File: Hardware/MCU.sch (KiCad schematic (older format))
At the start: 11 parts, among them J1 HDR, SW1 SW_Push, SW2 SW_Push, U5 ESP32-WROOM-32D

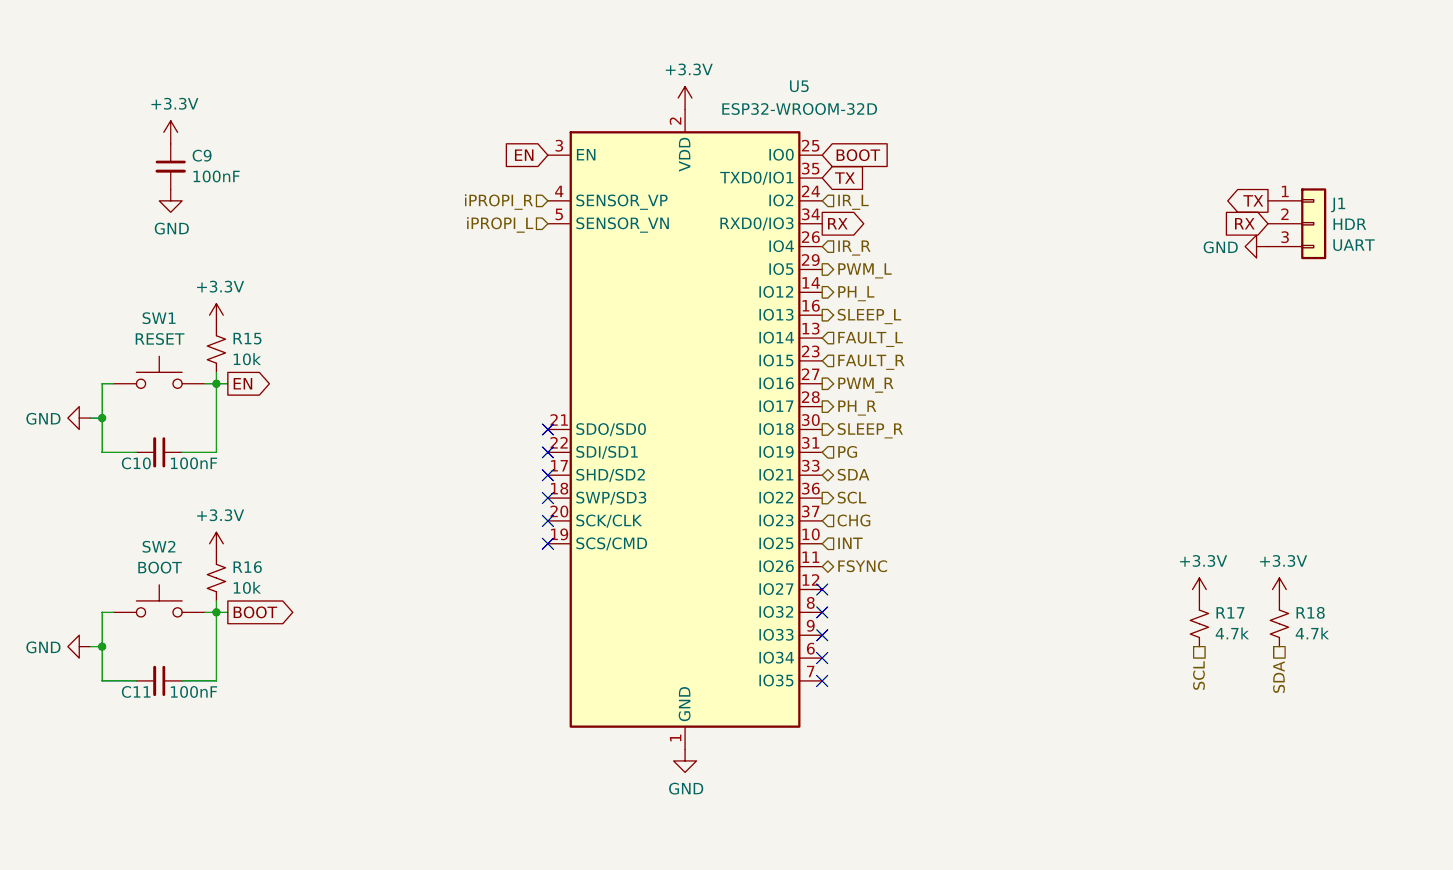
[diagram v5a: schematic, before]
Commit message: Schematic updated, USB comms circuit added
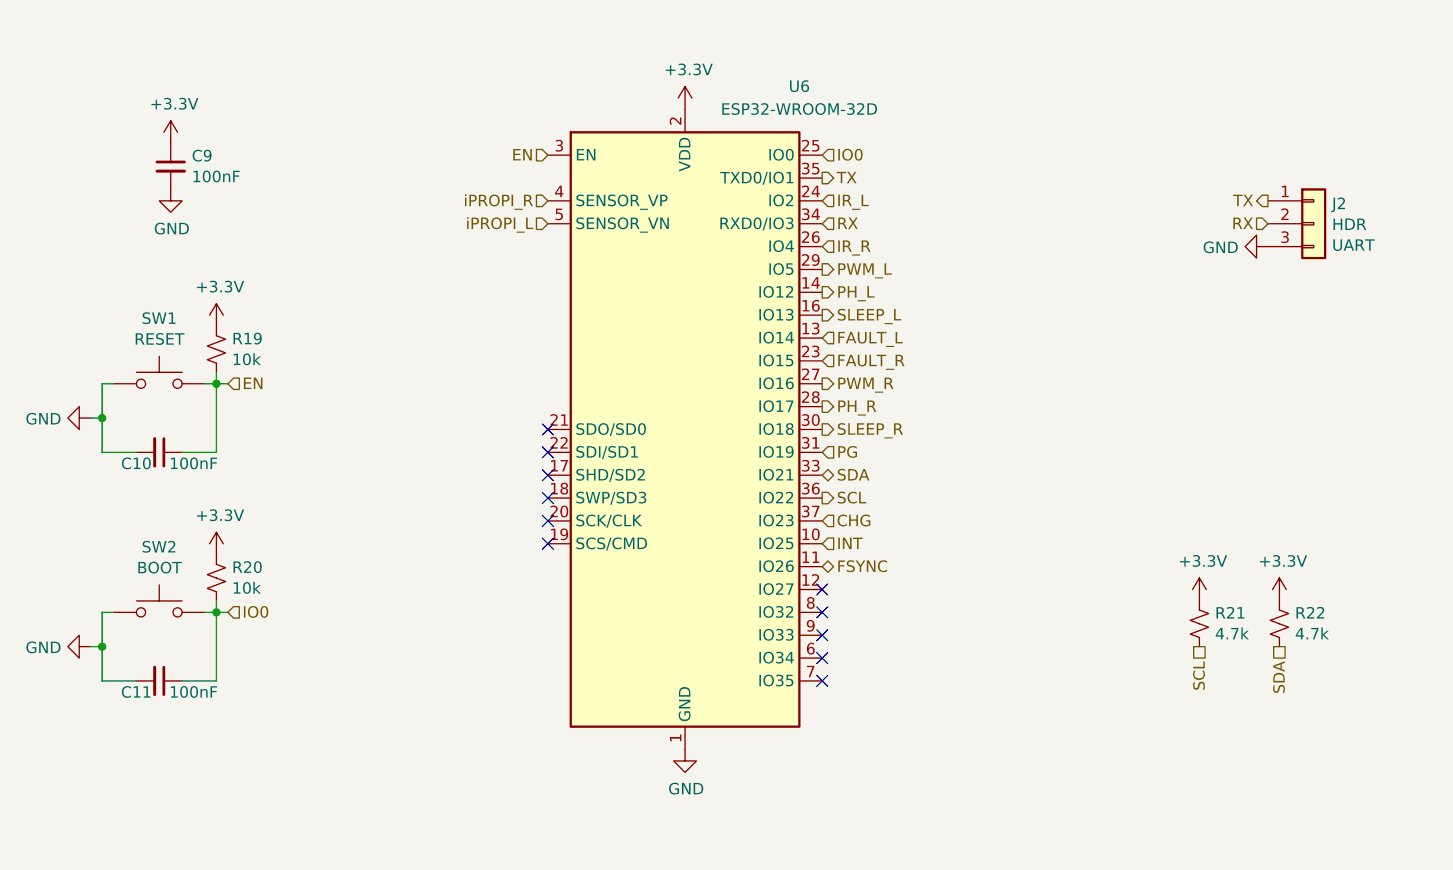
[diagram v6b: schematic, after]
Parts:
- J2: renamed from J1; footprint (none) -> Connector_PinSocket_2.54mm:PinSocket_1x03_P2.54mm_Vertical
- R21: renamed from R17; footprint Resistor_SMD:R_0603_1608Metric -> Resistor_SMD:R_0805_2012Metric
- R22: renamed from R18; footprint Resistor_SMD:R_0603_1608Metric -> Resistor_SMD:R_0805_2012Metric
- renumbered R15 to R19, R16 to R20, U5 to U6
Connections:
- net BOOT renamed IO0
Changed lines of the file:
@@
 $Descr A4 11693 8268
 encoding utf-8
-Sheet 6 9
+Sheet 6 11
 Title ""
 Date ""
@@
 AR Path="/5EA2026E/5FF09BD0" Ref="#PWR?"  Part="1"
 AR Path="/5FF09BD0" Ref="#PWR?"  Part="1"
-AR Path="/5FEFFC20/5FF09BD0" Ref="#PWR035"  Part="1"
-F 0 "#PWR035" H 3750 2400 50  0001 C CNN
+AR Path="/5FEFFC20/5FF09BD0" Ref="#PWR039"  Part="1"
+F 0 "#PWR039" H 3750 2400 50  0001 C CNN
 F 1 "+3.3V" H 3765 2723 50  0000 C CNN
 F 2 "" H 3750 2550 50  0001 C CNN
@@
 	1    0    0    -1
 $EndComp
-Text GLabel 4000 3600 2    50   Output ~ 0
-EN
 $Comp
 L Device:C_Small C?
@@
 Wire Wire Line
 	3450 4600 3500 4600
-Text GLabel 4000 4600 2    50   Output ~ 0
-BOOT
 NoConn ~ 5400 3800
 NoConn ~ 5400 3900
@@
 NoConn ~ 5400 4200
 NoConn ~ 5400 4300
-Text GLabel 5400 2600 0    50   Input ~ 0
-EN
-Text GLabel 6600 2600 2    50   Input ~ 0
-BOOT
-$Comp
-L power:GND #PWR044
+$Comp
+L power:GND #PWR048
 U 1 1 5FF09BF4
 P 6000 5200
-F 0 "#PWR044" H 6000 4950 50  0001 C CNN
+F 0 "#PWR048" H 6000 4950 50  0001 C CNN
 F 1 "GND" H 6005 5027 50  0000 C CNN
 F 2 "" H 6000 5200 50  0001 C CNN
@@
 AR Path="/5EA2026E/5FF09C08" Ref="#PWR?"  Part="1"
 AR Path="/5FF09C08" Ref="#PWR?"  Part="1"
-AR Path="/5FEFFC20/5FF09C08" Ref="#PWR036"  Part="1"
-F 0 "#PWR036" H 3750 2500 50  0001 C CNN
+AR Path="/5FEFFC20/5FF09C08" Ref="#PWR040"  Part="1"
+F 0 "#PWR040" H 3750 2500 50  0001 C CNN
 F 1 "GND" H 3755 2577 50  0000 C CNN
 F 2 "" H 3750 2750 50  0001 C CNN
@@
 AR Path="/5EA2026E/5FF09C14" Ref="#PWR?"  Part="1"
 AR Path="/5FF09C14" Ref="#PWR?"  Part="1"
-AR Path="/5FEFFC20/5FF09C14" Ref="#PWR038"  Part="1"
-F 0 "#PWR038" H 3950 3200 50  0001 C CNN
+AR Path="/5FEFFC20/5FF09C14" Ref="#PWR042"  Part="1"
+F 0 "#PWR042" H 3950 3200 50  0001 C CNN
 F 1 "+3.3V" H 3965 3523 50  0000 C CNN
 F 2 "" H 3950 3350 50  0001 C CNN
@@
 AR Path="/5EA2026E/5FF09C1A" Ref="R?"  Part="1"
 AR Path="/5FF09C1A" Ref="R?"  Part="1"
-AR Path="/5FEFFC20/5FF09C1A" Ref="R15"  Part="1"
-F 0 "R15" H 4018 3496 50  0000 L CNN
+AR Path="/5FEFFC20/5FF09C1A" Ref="R19"  Part="1"
+F 0 "R19" H 4018 3496 50  0000 L CNN
 F 1 "10k" H 4018 3405 50  0000 L CNN
 F 2 "Resistor_SMD:R_0805_2012Metric" H 3950 3450 50  0001 C CNN
@@
 	3950 3550 3950 3600
 $Comp
-L power:GND #PWR039
+L power:GND #PWR043
 U 1 1 5FF09C21
 P 3400 3750
-F 0 "#PWR039" H 3400 3500 50  0001 C CNN
+F 0 "#PWR043" H 3400 3500 50  0001 C CNN
 F 1 "GND" V 3405 3622 50  0000 R CNN
 F 2 "" H 3400 3750 50  0001 C CNN
@@
 	3450 3750 3450 3600
 $Comp
-L power:GND #PWR043
+L power:GND #PWR047
 U 1 1 5FF09C2A
 P 3400 4750
-F 0 "#PWR043" H 3400 4500 50  0001 C CNN
+F 0 "#PWR047" H 3400 4500 50  0001 C CNN
 F 1 "GND" V 3405 4622 50  0000 R CNN
 F 2 "" H 3400 4750 50  0001 C CNN
@@
 	3450 4750 3450 4600
 $Comp
-L power:+3.3V #PWR034
+L power:+3.3V #PWR038
 U 1 1 5FF09C33
 P 6000 2400
-F 0 "#PWR034" H 6000 2250 50  0001 C CNN
+F 0 "#PWR038" H 6000 2250 50  0001 C CNN
 F 1 "+3.3V" H 6015 2573 50  0000 C CNN
 F 2 "" H 6000 2400 50  0001 C CNN
@@
 $EndComp
 $Comp
-L Device:R_Small_US R18
+L Device:R_Small_US R22
 U 1 1 5FF09C39
 P 8600 4650
-F 0 "R18" H 8668 4696 50  0000 L CNN
+F 0 "R22" H 8668 4696 50  0000 L CNN
 F 1 "4.7k" H 8668 4605 50  0000 L CNN
-F 2 "Resistor_SMD:R_0603_1608Metric" H 8600 4650 50  0001 C CNN
+F 2 "Resistor_SMD:R_0805_2012Metric" H 8600 4650 50  0001 C CNN
 F 3 "~" H 8600 4650 50  0001 C CNN
 	1    8600 4650
@@
 $EndComp
 $Comp
-L Device:R_Small_US R17
+L Device:R_Small_US R21
 U 1 1 5FF09C3F
 P 8250 4650
-F 0 "R17" H 8318 4696 50  0000 L CNN
+F 0 "R21" H 8318 4696 50  0000 L CNN
 F 1 "4.7k" H 8318 4605 50  0000 L CNN
-F 2 "Resistor_SMD:R_0603_1608Metric" H 8250 4650 50  0001 C CNN
+F 2 "Resistor_SMD:R_0805_2012Metric" H 8250 4650 50  0001 C CNN
 F 3 "~" H 8250 4650 50  0001 C CNN
 	1    8250 4650
@@
 $EndComp
 $Comp
-L power:+3.3V #PWR041
+L power:+3.3V #PWR045
 U 1 1 5FF09C47
 P 8250 4550
-F 0 "#PWR041" H 8250 4400 50  0001 C CNN
+F 0 "#PWR045" H 8250 4400 50  0001 C CNN
 F 1 "+3.3V" H 8265 4723 50  0000 C CNN
 F 2 "" H 8250 4550 50  0001 C CNN
@@
 $EndComp
 $Comp
-L power:+3.3V #PWR042
+L power:+3.3V #PWR046
 U 1 1 5FF09C4D
 P 8600 4550
-F 0 "#PWR042" H 8600 4400 50  0001 C CNN
+F 0 "#PWR046" H 8600 4400 50  0001 C CNN
 F 1 "+3.3V" H 8615 4723 50  0000 C CNN
 F 2 "" H 8600 4550 50  0001 C CNN
@@
 AR Path="/5EA2026E/5FF09C78" Ref="#PWR?"  Part="1"
 AR Path="/5FF09C78" Ref="#PWR?"  Part="1"
-AR Path="/5FEFFC20/5FF09C78" Ref="#PWR040"  Part="1"
-F 0 "#PWR040" H 3950 4200 50  0001 C CNN
+AR Path="/5FEFFC20/5FF09C78" Ref="#PWR044"  Part="1"
+F 0 "#PWR044" H 3950 4200 50  0001 C CNN
 F 1 "+3.3V" H 3965 4523 50  0000 C CNN
 F 2 "" H 3950 4350 50  0001 C CNN
@@
 AR Path="/5EA2026E/5FF09C7E" Ref="R?"  Part="1"
 AR Path="/5FF09C7E" Ref="R?"  Part="1"
-AR Path="/5FEFFC20/5FF09C7E" Ref="R16"  Part="1"
-F 0 "R16" H 4018 4496 50  0000 L CNN
+AR Path="/5FEFFC20/5FF09C7E" Ref="R20"  Part="1"
+F 0 "R20" H 4018 4496 50  0000 L CNN
 F 1 "10k" H 4018 4405 50  0000 L CNN
 F 2 "Resistor_SMD:R_0805_2012Metric" H 3950 4450 50  0001 C CNN
@@
 	3950 4550 3950 4600
 $Comp
-L Connector_Generic:Conn_01x03 J1
+L Connector_Generic:Conn_01x03 J2
 U 1 1 5FF09C86
 P 8750 2900
-F 0 "J1" H 8830 2987 50  0000 L CNN
+F 0 "J2" H 8830 2987 50  0000 L CNN
 F 1 "HDR" H 8830 2896 50  0000 L CNN
-F 2 "" H 8750 2900 50  0001 C CNN
+F 2 "Connector_PinSocket_2.54mm:PinSocket_1x03_P2.54mm_Vertical" H 8750 2900 50  0001 C CNN
 F 3 "~" H 8750 2900 50  0001 C CNN
 F 4 "UART" H 8830 2805 50  0000 L CNN "Field4"
@@
 	1    0    0    -1
 $EndComp
-Text GLabel 6600 2900 2    50   Output ~ 0
-RX
-Text GLabel 6600 2700 2    50   Input ~ 0
-TX
-Text GLabel 8550 2900 0    50   Input ~ 0
-RX
-Text GLabel 8550 2800 0    50   Output ~ 0
-TX
-$Comp
-L power:GND #PWR037
+$Comp
+L power:GND #PWR041
 U 1 1 5FF09C90
 P 8550 3000
-F 0 "#PWR037" H 8550 2750 50  0001 C CNN
+F 0 "#PWR041" H 8550 2750 50  0001 C CNN
 F 1 "GND" V 8555 2872 50  0000 R CNN
 F 2 "" H 8550 3000 50  0001 C CNN
@@
 NoConn ~ 6600 4900
 $Comp
-L RF_Module:ESP32-WROOM-32D U5
+L RF_Module:ESP32-WROOM-32D U6
 U 1 1 607032D0
 P 6000 3800
-F 0 "U5" H 6500 5300 50  0000 C CNN
+F 0 "U6" H 6500 5300 50  0000 C CNN
 F 1 "ESP32-WROOM-32D" H 6500 5200 50  0000 C CNN
 F 2 "RF_Module:ESP32-WROOM-32" H 6000 2300 50  0001 C CNN
@@
 Text HLabel 8600 4750 3    50   UnSpc ~ 0
 SDA
+Text HLabel 6600 2900 2    50   Input ~ 0
+RX
+Text HLabel 6600 2700 2    50   Output ~ 0
+TX
+Text HLabel 6600 2600 2    50   Input ~ 0
+IO0
+Text HLabel 5400 2600 0    50   Input ~ 0
+EN
+Text HLabel 4000 3600 2    50   Input ~ 0
+EN
+Text HLabel 4000 4600 2    50   Input ~ 0
+IO0
+Text HLabel 8550 2800 0    50   Output ~ 0
+TX
+Text HLabel 8550 2900 0    50   Input ~ 0
+RX
 $EndSCHEMATC

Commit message: PCB design started
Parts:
- removed R21, R22: 4.7k, Resistor_SMD:R_0805_2012Metric, symbol Device:R_Small_US
- added J3: JTAG, Connector_PinHeader_1.27mm:PinHeader_2x05_P1.27mm_Vertical_SMD, symbol Connector_Generic:Conn_02x05_Odd_Even
- C10: renamed from C11; symbol Device:C_Small -> Roverette-rescue:C_Small-Device
- C11: renamed from C9; symbol Device:C_Small -> Roverette-rescue:C_Small-Device
- C9: renamed from C10; symbol Device:C_Small -> Roverette-rescue:C_Small-Device
- J1: renamed from J2; footprint Connector_PinSocket_2.54mm:PinSocket_1x03_P2.54mm_Vertical -> Connector_PinHeader_2.54mm:PinHeader_1x03_P2.54mm_Vertical; symbol Connector_Generic:Conn_01x03 -> Roverette-rescue:Conn_01x03-Connector_Generic
- R19, R20: symbol Device:R_Small_US -> Roverette-rescue:R_Small_US-Device
- SW1, SW2: symbol Switch:SW_Push -> Roverette-rescue:SW_Push-Switch
- U5: renamed from U6; symbol RF_Module:ESP32-WROOM-32D -> Roverette-rescue:ESP32-WROOM-32D-RF_Module
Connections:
- net FSYNC is gone; now on net CHG: U5.11 (IO26)
- net INT is gone; now on net PG: U5.10 (IO25)
- net SCL is gone; now on net FAULT_L: U5.36 (IO22)
- net SDA is gone; now on net SLEEP_L: U5.33 (IO21)
- net +3V3: now also J3.1 (Pin_1)
- net CHG: no longer U5.37 (IO23)
- net EN: now also J3.10 (Pin_10)
- net FAULT_L: no longer U5.13 (IO14)
- net FAULT_R: now also U5.37 (IO23); no longer U5.23 (IO15)
- net GND: now also J3.3 (Pin_3), J3.5 (Pin_5), J3.9 (Pin_9)
- net PG: no longer U5.31 (IO19)
- net PH_L: now also U5.31 (IO19); no longer U5.14 (IO12)
- net SLEEP_L: no longer U5.16 (IO13)
- net IO27: now reaches U5.12 (IO27)
- net SDH: now reaches U5.17 (SHD/SD2)
- net SWP: now reaches U5.18 (SWP/SD3)
- net SCS: now reaches U5.19 (SCS/CMD)
- net SCK: now reaches U5.20 (SCK/CLK)
- net SD0: now reaches U5.21 (SDO/SD0)
- net SDI: now reaches U5.22 (SDI/SD1)
- net IO34: now reaches U5.6 (IO34)
- net IO35: now reaches U5.7 (IO35)
- net IO32: now reaches U5.8 (IO32)
- net IO33: now reaches U5.9 (IO33)
- new net TCK: J3.4 (Pin_4), U5.13 (IO14)
- new net TDI: J3.8 (Pin_8), U5.16 (IO13)
- new net TDO: J3.6 (Pin_6), U5.14 (IO12)
- new net TMS: J3.2 (Pin_2), U5.23 (IO15)
- no-connect marks 11 -> 12
